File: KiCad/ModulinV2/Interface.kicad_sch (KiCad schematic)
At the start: 2 parts, among them IC2 ADS7866IDBVT, IC3 ADS7866IDBVT

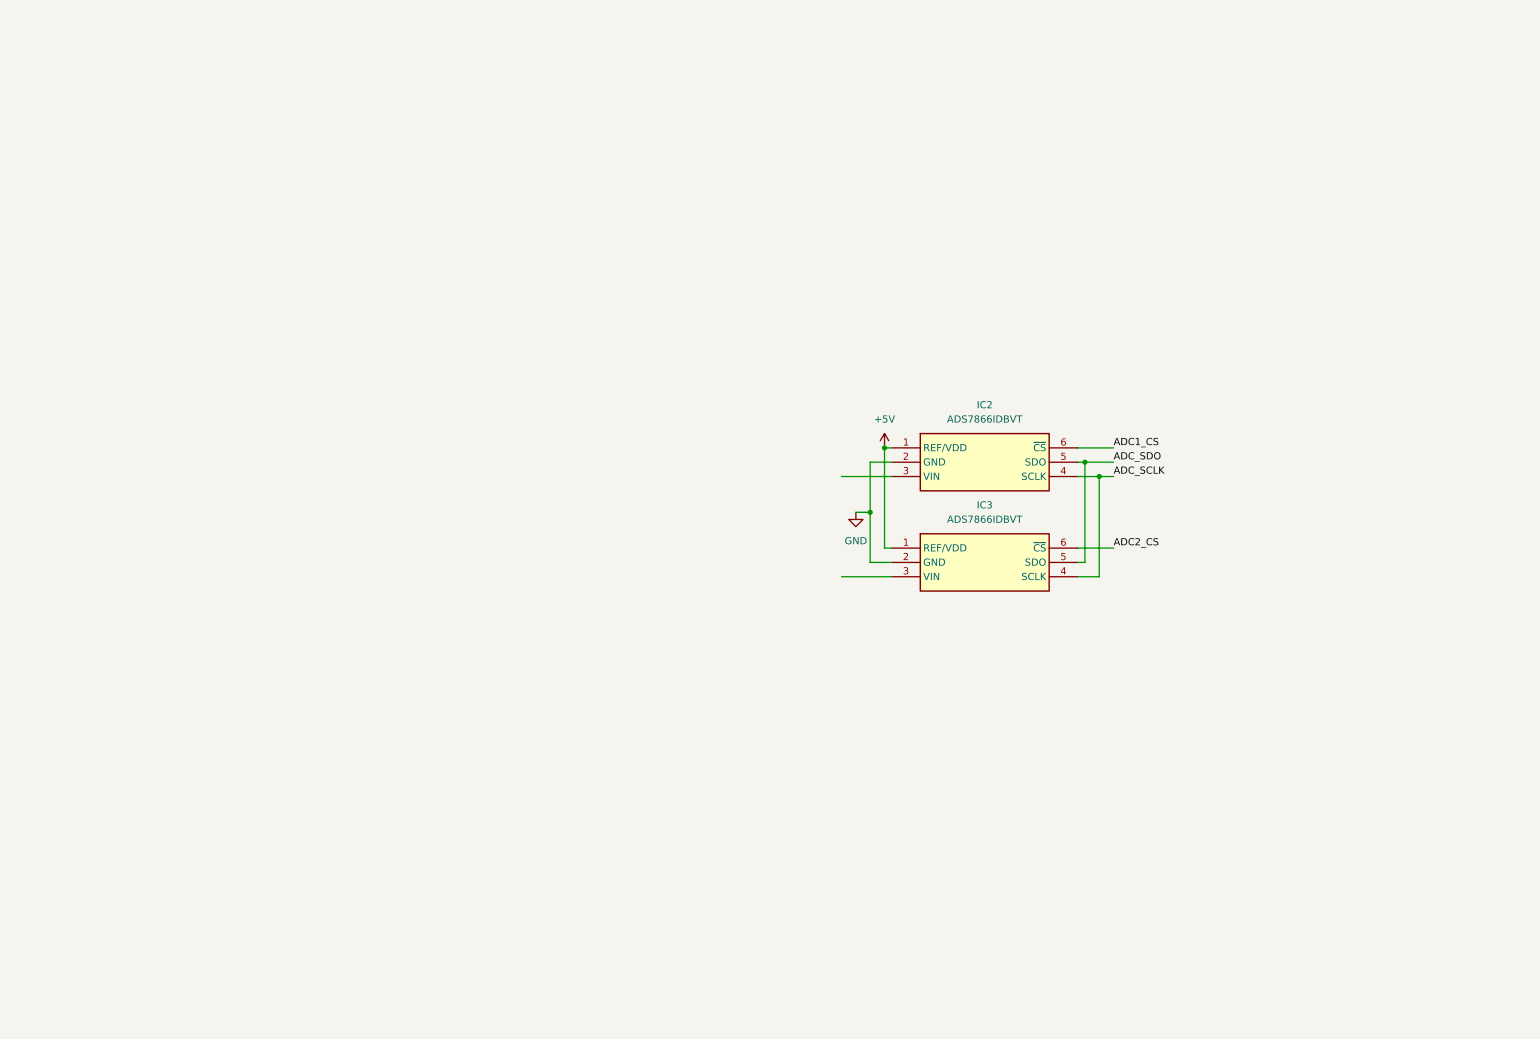
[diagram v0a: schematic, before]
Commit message: Added initial schematic and components for interface
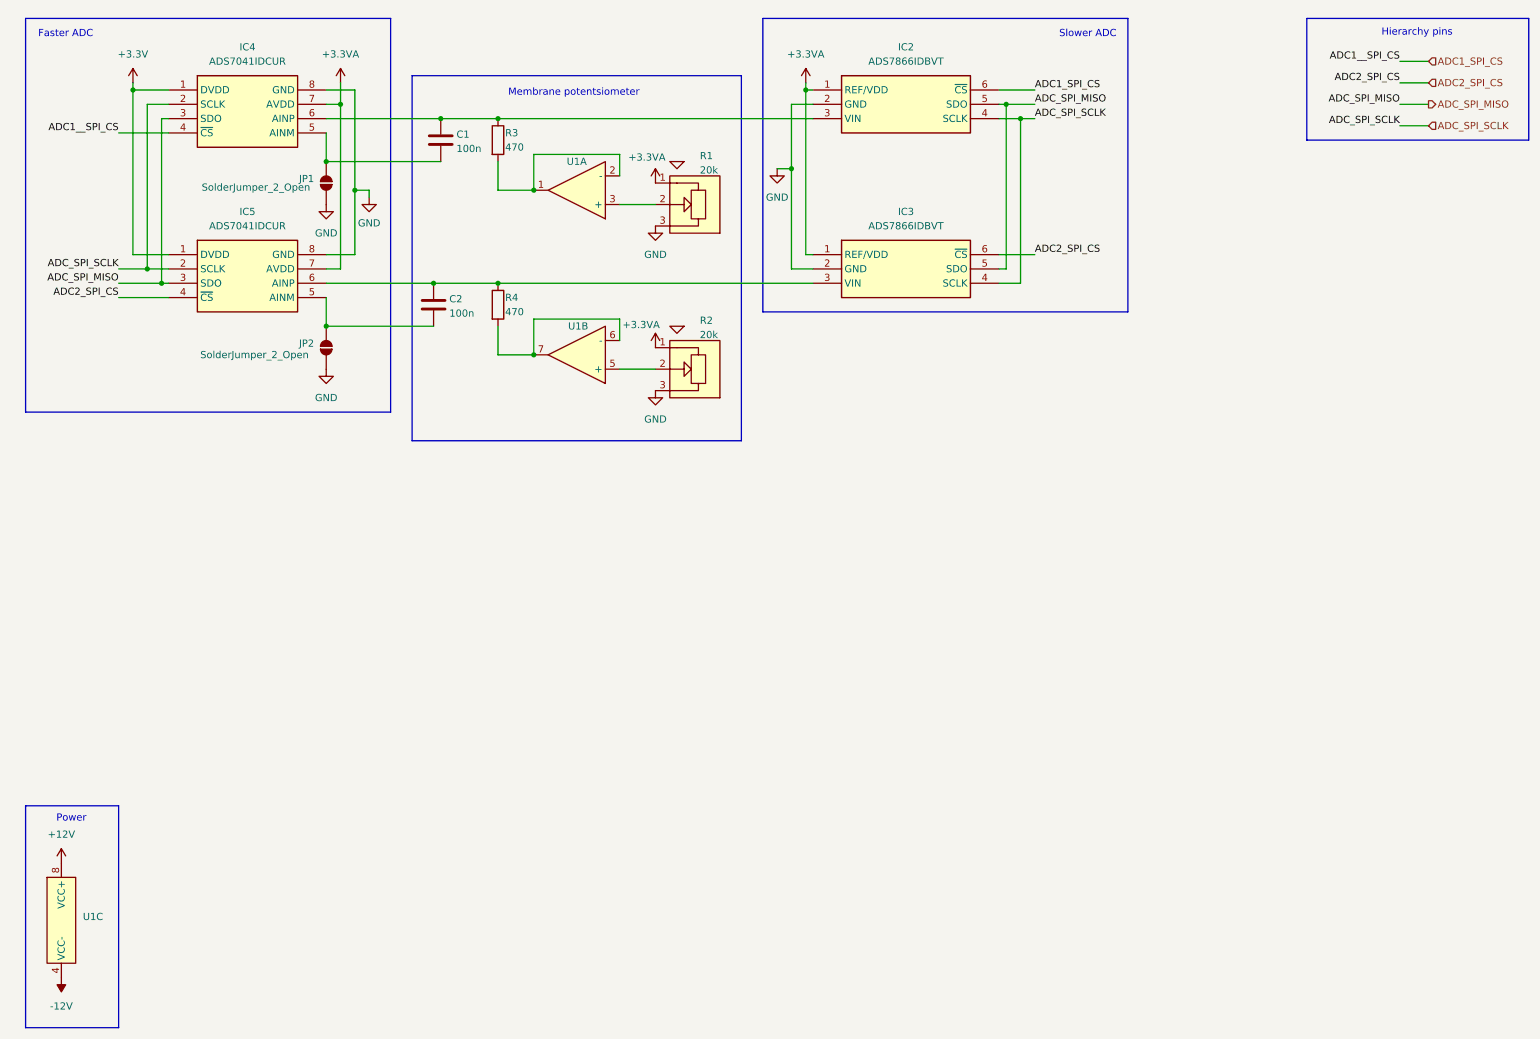
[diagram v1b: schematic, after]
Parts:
- added C1, C2: 100n, symbol Device:C
- added IC4, IC5: ADS7041IDCUR, Modulin:SOP50P310X90-8N, symbol ADS7041IDCUR:ADS7041IDCUR
- added JP1, JP2: SolderJumper_2_Open, Jumper:SolderJumper-2_P1.3mm_Open_TrianglePad1.0x1.5mm, symbol Jumper:SolderJumper_2_Open
- added R1, R2: 20k, TSP-L-0400-203-1%-ST:TSP-L-0400-203-1%-ST, symbol TSP-L-0400-203-1%-ST:TSP-L-0400-203-1%-ST
- added R3, R4: 470, symbol Device:R
- added U1: ~, TL072HIDDFR:SOT65P280X110-8N, symbol TL072HIDDFR:TL072HIDDFR_2
- IC2, IC3: footprint SOT95P280X145-6N -> Modulin:SOT95P280X145-6N
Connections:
- net GND: now also IC4.8 (GND), IC5.8 (GND), JP1.1 (A), JP2.1 (A), R1.3, R2.3
- net at IC3.3 (VIN): now also C2.1, IC5.6 (AINP), R4.1
- net at IC2.3 (VIN): now also C1.1, IC4.6 (AINP), R3.1
- net +5V renamed +3.3VA
- net +3.3VA: now also IC4.7 (AVDD), IC5.7 (AVDD), R1.1, R2.1
- net ADC1_CS renamed ADC1_SPI_CS
- net ADC1_SPI_CS: now also IC4.4 (~{CS})
- net ADC2_CS renamed ADC2_SPI_CS
- net ADC2_SPI_CS: now also IC5.4 (~{CS})
- net ADC_SCLK renamed ADC_SPI_SCLK
- net ADC_SPI_SCLK: now also IC4.2 (SCLK), IC5.2 (SCLK)
- net ADC_SDO renamed ADC_SPI_MISO
- net ADC_SPI_MISO: now also IC4.3 (SDO), IC5.3 (SDO)
- new net: R2.2, U1.5 (+)
- new net: R4.2, U1.6 (-), U1.7
- new net: R3.2, U1.1, U1.2 (-)
- new net: R1.2, U1.3 (+)
- new net: C1.2, IC4.5 (AINM), JP1.2 (B)
- new net: C2.2, IC5.5 (AINM), JP2.2 (B)
- new net +12V: U1.8 (VCC+)
- new net +3.3V: IC4.1 (DVDD), IC5.1 (DVDD)
- new net -12V: U1.4 (VCC-)
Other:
- note added: "Faster ADC"
- note added: "Hierarchy pins"
- note added: "Membrane potentsiometer"
- note added: "Power"
- note added: "Slower ADC"
- moved on the sheet: IC2, IC3

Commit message: Semi-finished interface schematic
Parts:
- removed unit 3 of U1
- added C14, C16: 1u, symbol Device:C
- added C15, C17, C18, C19: 100n, symbol Device:C
- added IC6, IC7: DAC60501ZDGSR, SOP50P490X110-10N, symbol DAC60501ZDGSR:DAC60501ZDGSR
- added R10, R11, R12, R13, R8, R9: R, symbol Device:R
- added R14, R15: 1k, symbol Device:R
- added R16, R17: 470, symbol Device:R
- added R6, R7: ~, symbol SEN0299:SEN0299
- added RV1, RV2: R_Potentiometer_Trim, symbol Device:R_Potentiometer_Trim
- added U2, U3: ~, symbol TL072HIDDFR:TL072HIDDFR_2
- U1: footprint TL072HIDDFR:SOT65P280X110-8N -> (none)
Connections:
- net +12V: now also U1.8 (V+), RV1.1, RV2.1, U2.8 (V+), U3.8 (V+)
- net +3.3V: now also C14.2, C16.2, IC6.1 (VDD), IC7.1 (VDD)
- net +3.3VA: now also R6.2, R7.2
- net -12V: now also U1.4 (V-), RV1.3, RV2.3, U2.4 (V-), U3.4 (V-)
- net GND: now also C14.1, C15.2, C16.1, C17.2, C18.2, C19.2, IC6.4 (AGND), IC7.4 (AGND), R14.2, R15.2, R8.2, R9.2
- net at R2.2: now also U1.3 (+); no longer U1.5 (+)
- net at U1.6 (-), U1.7: now also R3.2; no longer R4.2
- net at U1.1, U1.2 (-): now also R4.2; no longer R3.2
- net at R1.2: now also U1.5 (+); no longer U1.3 (+)
- new net: R17.1, R6.1, R8.1
- new net: R16.1, R7.1, R9.1
- new net: C18.1, R16.2, U3.3 (+), U3.6 (-)
- new net: R11.1, RV1.2
- new net: R10.1, R11.2, U3.5 (+)
- new net: IC7.5 (SPI2C), R15.1
- new net: C19.1, R17.2, U2.3 (+), U2.6 (-)
- new net: IC6.5 (SPI2C), R14.1
- new net: R12.1, RV2.2
- new net: R12.2, R13.1, U2.5 (+)
- new net +5V: C15.1, C17.1, IC6.10 (VREFIO), IC7.10 (VREFIO)
- new net DAC1_SPI_CS: IC6.7 (~{SYNC}/A0)
- new net DAC1_SPI_MOSI: IC6.8 (SDIN/SDA), IC7.8 (SDIN/SDA)
- new net DAC2_SPI_CS: IC7.7 (~{SYNC}/A0)
- new net DAC_SPI_CLK: IC6.6 (SCLK/SCL), IC7.6 (SCLK/SCL)
- new net INTERFACE_PITCH_CV1: IC6.2 (VOUT)
- new net INTERFACE_PITCH_CV2: IC7.2 (VOUT)
- new net NOTE_TRIG1: R13.2, U2.7
- new net NOTE_TRIG2: R10.2, U3.7
- new net PRESSURE_CV1: U2.1, U2.2 (-)
- new net PRESSURE_CV2: U3.1, U3.2 (-)
- no-connect marks 0 -> 4
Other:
- note added: "Membrane potentsiometers"
- note added: "Output 1"
- note added: "Output 2"
- note added: "Pressure sensor 1"
- note added: "Pressure sensor 2"
- note removed: "Membrane potentsiometer"
- note removed: "Power"
- moved on the sheet: C1, C2, IC2, IC3, IC4, IC5, JP1, JP2, R1, R2, R3, R4

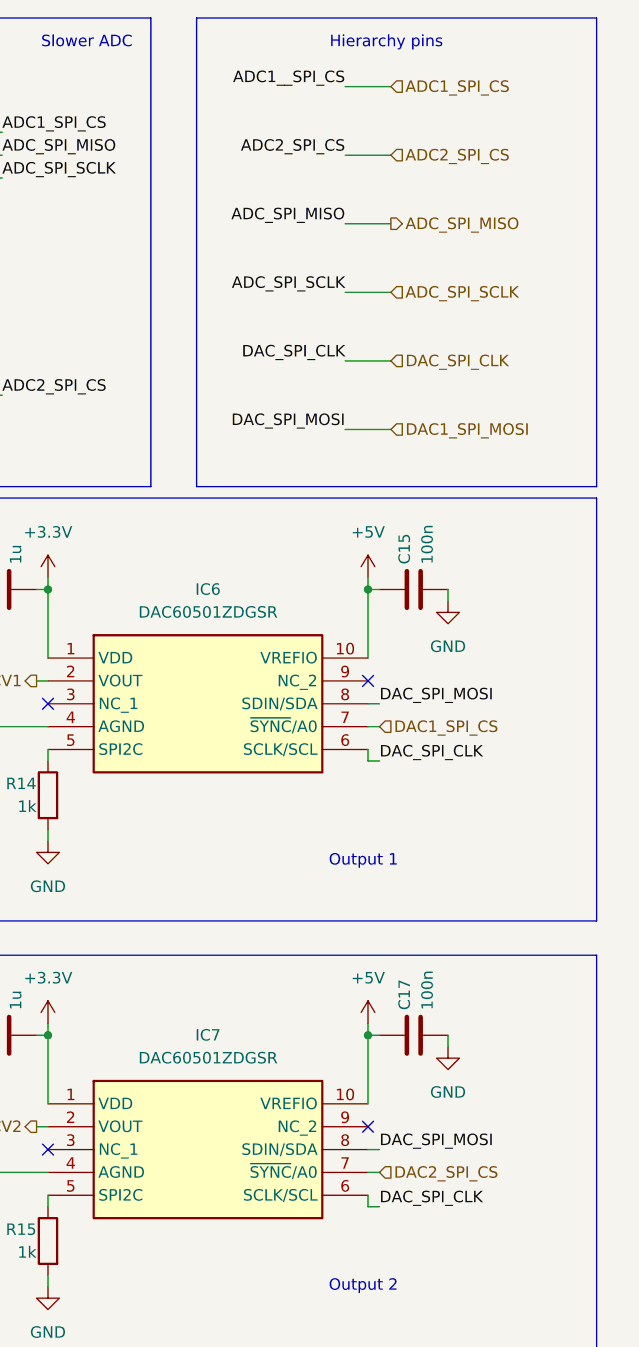
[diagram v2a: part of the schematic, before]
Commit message: Added CubeIDE folder and mapped out initial SPI pins
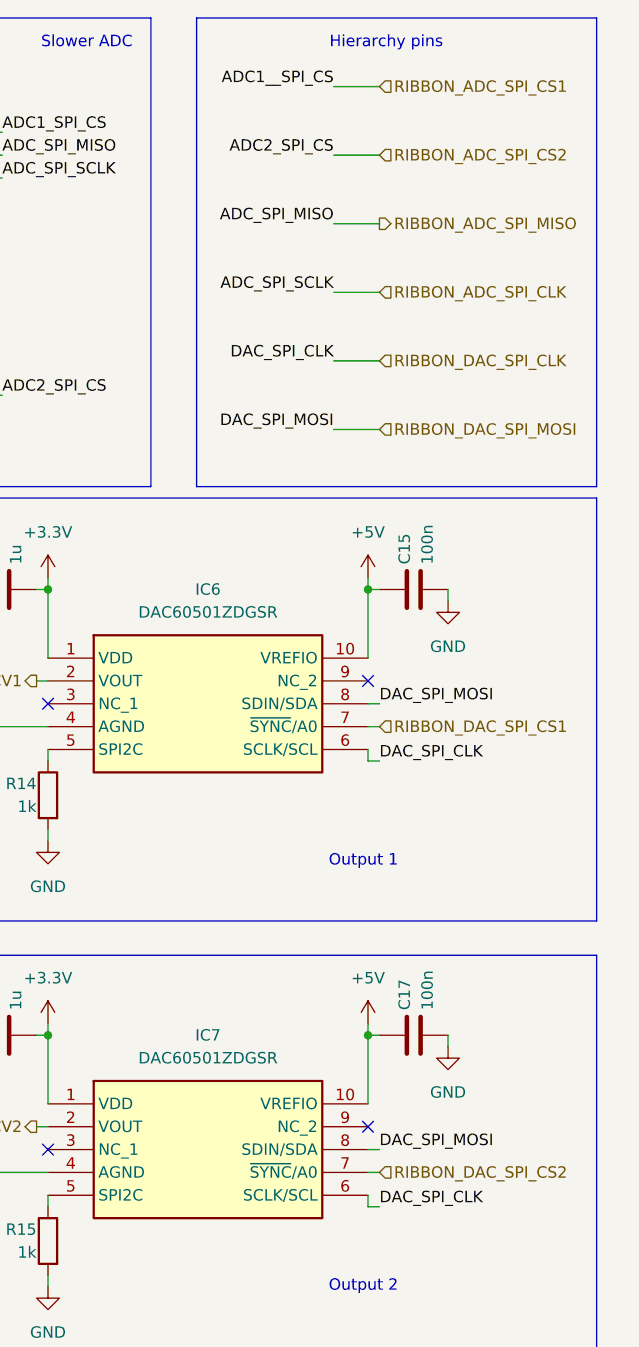
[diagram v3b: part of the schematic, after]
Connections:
- net ADC1_SPI_CS: no longer IC4.4 (~{CS})
- net ADC2_SPI_CS renamed RIBBON_ADC_SPI_CS2
- net ADC_SPI_MISO renamed RIBBON_ADC_SPI_MISO
- net ADC_SPI_SCLK renamed RIBBON_ADC_SPI_CLK
- net DAC1_SPI_CS renamed RIBBON_DAC_SPI_CS1
- net DAC1_SPI_MOSI renamed RIBBON_DAC_SPI_MOSI
- net DAC2_SPI_CS renamed RIBBON_DAC_SPI_CS2
- net DAC_SPI_CLK renamed RIBBON_DAC_SPI_CLK
- new net RIBBON_ADC_SPI_CS1: IC4.4 (~{CS})
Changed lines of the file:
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@@
 	(wire
 		(pts
-			(xy 243.84 45.72) (xy 248.92 45.72)
+			(xy 242.57 45.72) (xy 247.65 45.72)
 		)
 		(stroke
@@
 	(wire
 		(pts
-			(xy 243.84 53.34) (xy 248.92 53.34)
+			(xy 242.57 53.34) (xy 247.65 53.34)
 		)
 		(stroke
@@
 	(wire
 		(pts
-			(xy 243.84 38.1) (xy 248.92 38.1)
+			(xy 242.57 38.1) (xy 247.65 38.1)
 		)
 		(stroke
@@
 	(wire
 		(pts
-			(xy 243.84 60.96) (xy 248.92 60.96)
+			(xy 242.57 60.96) (xy 247.65 60.96)
 		)
 		(stroke
@@
 	(wire
 		(pts
-			(xy 243.84 30.48) (xy 248.92 30.48)
+			(xy 242.57 30.48) (xy 247.65 30.48)
 		)
 		(stroke
@@
 	(wire
 		(pts
-			(xy 243.84 22.86) (xy 248.92 22.86)
+			(xy 242.57 22.86) (xy 247.65 22.86)
 		)
 		(stroke
@@
 	)
 	(label "DAC_SPI_CLK"
-		(at 243.84 53.34 180)
+		(at 242.57 53.34 180)
 		(effects
 			(font
@@
 	)
 	(label "ADC2_SPI_CS"
-		(at 243.84 30.48 180)
+		(at 242.57 30.48 180)
 		(effects
 			(font
@@
 	)
 	(label "ADC_SPI_MISO"
-		(at 243.84 38.1 180)
+		(at 242.57 38.1 180)
 		(effects
 			(font
@@
 	)
 	(label "DAC_SPI_MOSI"
-		(at 243.84 60.96 180)
+		(at 242.57 60.96 180)
 		(effects
 			(font
@@
 	)
 	(label "ADC_SPI_SCLK"
-		(at 243.84 45.72 180)
+		(at 242.57 45.72 180)
 		(effects
 			(font
@@
 	)
 	(label "ADC1__SPI_CS"
-		(at 243.84 22.86 180)
+		(at 242.57 22.86 180)
 		(effects
 			(font
@@
 		)
 	)
-	(hierarchical_label "ADC1_SPI_CS"
+	(hierarchical_label "RIBBON_ADC_SPI_CS1"
 		(shape input)
-		(at 248.92 22.86 0)
+		(at 247.65 22.86 0)
 		(effects
 			(font
@@
 		)
 	)
-	(hierarchical_label "ADC_SPI_SCLK"
+	(hierarchical_label "RIBBON_ADC_SPI_CLK"
 		(shape input)
-		(at 248.92 45.72 0)
+		(at 247.65 45.72 0)
 		(effects
 			(font
@@
 		)
 	)
-	(hierarchical_label "DAC_SPI_CLK"
+	(hierarchical_label "RIBBON_DAC_SPI_CLK"
 		(shape input)
-		(at 248.92 53.34 0)
+		(at 247.65 53.34 0)
 		(effects
 			(font
@@
 		)
 	)
-	(hierarchical_label "ADC2_SPI_CS"
+	(hierarchical_label "RIBBON_ADC_SPI_CS2"
 		(shape input)
-		(at 248.92 30.48 0)
+		(at 247.65 30.48 0)
 		(effects
 			(font
@@
 		)
 	)
-	(hierarchical_label "ADC_SPI_MISO"
+	(hierarchical_label "RIBBON_ADC_SPI_MISO"
 		(shape output)
-		(at 248.92 38.1 0)
+		(at 247.65 38.1 0)
 		(effects
 			(font
@@
 		)
 	)
-	(hierarchical_label "DAC2_SPI_CS"
+	(hierarchical_label "RIBBON_DAC_SPI_CS2"
 		(shape input)
 		(at 247.65 143.51 0)
@@
 		)
 	)
-	(hierarchical_label "DAC1_SPI_MOSI"
+	(hierarchical_label "RIBBON_DAC_SPI_MOSI"
 		(shape input)
-		(at 248.92 60.96 0)
+		(at 247.65 60.96 0)
 		(effects
 			(font
@@
 		)
 	)
-	(hierarchical_label "DAC1_SPI_CS"
+	(hierarchical_label "RIBBON_DAC_SPI_CS1"
 		(shape input)
 		(at 247.65 93.98 0)
